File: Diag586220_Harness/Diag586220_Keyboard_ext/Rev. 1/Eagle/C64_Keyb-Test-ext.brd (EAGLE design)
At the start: 22 x 55 mm, 16 parts, among them IC1 4066N, IC2 4066N, J1 BL1-85AXX-20U, Q1 BC547B

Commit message: Silk Screen Update
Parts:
- added U$19: OPEN_SOURCE_HW, Logo:OPENHW
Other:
- board text added: "http://github.com/svenpetersen1965"
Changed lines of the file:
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@@
 <layer number="21" name="tPlace" color="7" fill="1" visible="yes" active="yes"/>
 <layer number="22" name="bPlace" color="7" fill="1" visible="no" active="yes"/>
-<layer number="23" name="tOrigins" color="15" fill="1" visible="yes" active="yes"/>
+<layer number="23" name="tOrigins" color="15" fill="1" visible="no" active="yes"/>
 <layer number="24" name="bOrigins" color="15" fill="1" visible="no" active="yes"/>
 <layer number="25" name="tNames" color="7" fill="1" visible="yes" active="yes"/>
@@
 <layer number="45" name="Holes" color="7" fill="1" visible="yes" active="yes"/>
 <layer number="46" name="Milling" color="3" fill="1" visible="no" active="yes"/>
-<layer number="47" name="Measures" color="7" fill="1" visible="no" active="yes"/>
+<layer number="47" name="Measures" color="7" fill="1" visible="yes" active="yes"/>
 <layer number="48" name="Document" color="5" fill="1" visible="yes" active="yes"/>
 <layer number="49" name="Reference" color="7" fill="1" visible="yes" active="yes"/>
@@
 <layer number="250" name="Descript" color="7" fill="1" visible="no" active="no"/>
 <layer number="251" name="SMDround" color="7" fill="1" visible="no" active="no"/>
+<layer number="252" name="BR-BS" color="7" fill="1" visible="no" active="yes"/>
+<layer number="253" name="BR-LS" color="7" fill="1" visible="no" active="yes"/>
 <layer number="254" name="OrgLBR" color="7" fill="1" visible="no" active="no"/>
 <layer number="255" name="Accent" color="7" fill="1" visible="yes" active="yes"/>
@@
 <text x="15.24" y="2.69875" size="1.016" layer="25">4k7</text>
 <text x="15.24" y="0.3175" size="1.016" layer="25">1k</text>
+<text x="2.54" y="39.52875" size="1.016" layer="22" rot="MR270">http://github.com/svenpetersen1965</text>
 </plain>
 <attributes>
@@
 <attribute name="VALUE" x="6.82625" y="51.1175" size="1.27" layer="27"/>
 </element>
+<element name="U$19" library="Logo" package="OPENHW" value="OPEN_SOURCE_HW" x="17.30375" y="3.96875" smashed="yes" rot="MR0"/>
 </elements>
 <signals>

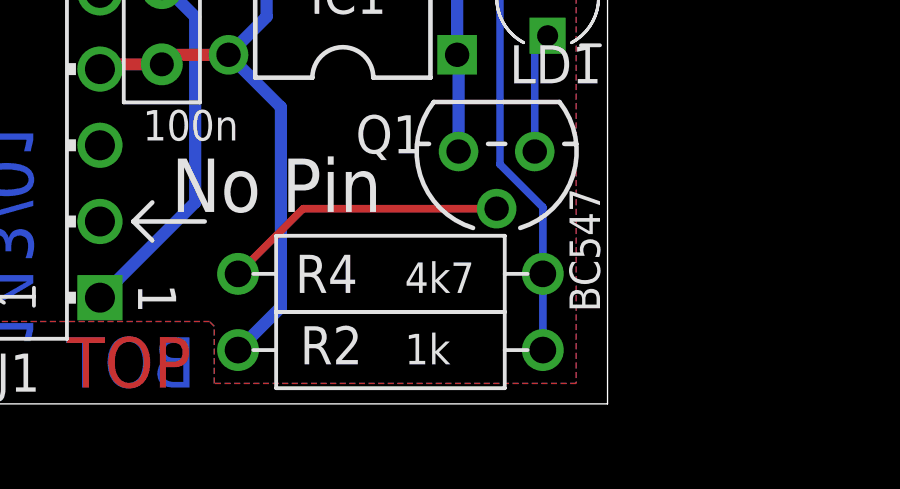
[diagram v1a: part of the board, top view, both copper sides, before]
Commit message: BOM v1.1
R2 and R4 values are changed
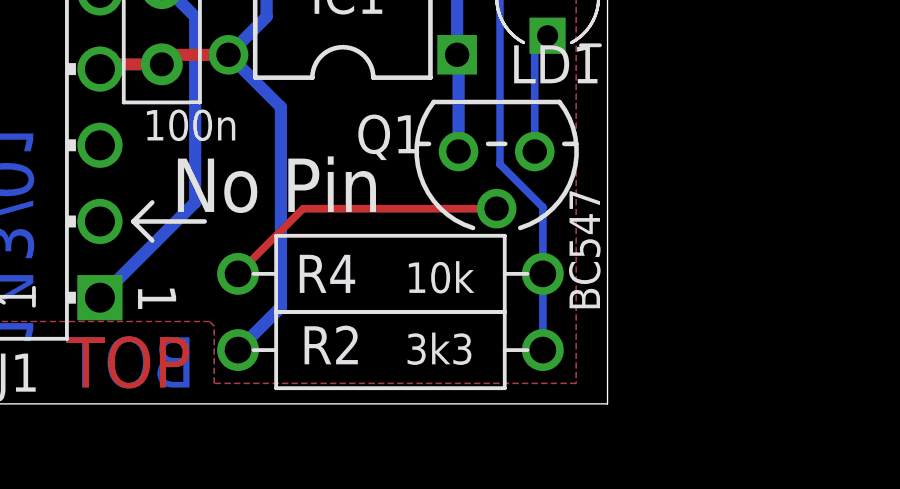
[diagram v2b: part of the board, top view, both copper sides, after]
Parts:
- R2: value 1k -> 3k3
- R4: value 4k7 -> 10k
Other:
- board text added: "3k3"
- board text removed: "1k"
- board text removed: "4k7"
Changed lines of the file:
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@@
 <?xml version="1.0" encoding="utf-8"?>
 <!DOCTYPE eagle SYSTEM "eagle.dtd">
-<eagle version="9.5.2">
+<eagle version="9.6.2">
 <drawing>
 <settings>
@@
 <layer number="21" name="tPlace" color="7" fill="1" visible="yes" active="yes"/>
 <layer number="22" name="bPlace" color="7" fill="1" visible="no" active="yes"/>
-<layer number="23" name="tOrigins" color="15" fill="1" visible="no" active="yes"/>
+<layer number="23" name="tOrigins" color="15" fill="1" visible="yes" active="yes"/>
 <layer number="24" name="bOrigins" color="15" fill="1" visible="no" active="yes"/>
 <layer number="25" name="tNames" color="7" fill="1" visible="yes" active="yes"/>
@@
 <layer number="28" name="bValues" color="7" fill="1" visible="no" active="yes"/>
 <layer number="29" name="tStop" color="7" fill="3" visible="no" active="yes"/>
-<layer number="30" name="bStop" color="7" fill="6" visible="no" active="yes"/>
+<layer number="30" name="bStop" color="7" fill="6" visible="yes" active="yes"/>
 <layer number="31" name="tCream" color="7" fill="4" visible="no" active="yes"/>
 <layer number="32" name="bCream" color="7" fill="5" visible="no" active="yes"/>
@@
 <text x="13.97" y="27.14625" size="1.016" layer="25" rot="R90">100n</text>
 <text x="21.74875" y="2.06375" size="1.016" layer="25" rot="R90">BC547</text>
-<text x="15.24" y="2.69875" size="1.016" layer="25">4k7</text>
-<text x="15.24" y="0.3175" size="1.016" layer="25">1k</text>
+<text x="15.24" y="2.69875" size="1.016" layer="25">10k</text>
+<text x="15.24" y="0.3175" size="1.016" layer="25">3k3</text>
 <text x="2.54" y="39.52875" size="1.016" layer="22" rot="MR270">http://github.com/svenpetersen1965</text>
 </plain>
@@
 <attribute name="VALUE" x="14.605" y="50.32375" size="1.27" layer="27" rot="R180"/>
 </element>
-<element name="R2" library="DISCRETE" package="R-10" value="1k" x="14.76375" y="0.79375" smashed="yes" rot="R180">
+<element name="R2" library="DISCRETE" package="R-10" value="3k3" x="14.76375" y="0.79375" smashed="yes" rot="R180">
 <attribute name="NAME" x="11.7475" y="0.3175" size="1.27" layer="25"/>
 <attribute name="VALUE" x="17.93875" y="1.42875" size="1.27" layer="27" rot="R180"/>
@@
 </element>
 <element name="U$17" library="Logo" package="SVEN_TAG" value="" x="2.06375" y="23.97125" smashed="yes"/>
-<element name="R4" library="DISCRETE" package="R-10" value="4k7" x="14.76375" y="3.33375" smashed="yes">
+<element name="R4" library="DISCRETE" package="R-10" value="10k" x="14.76375" y="3.33375" smashed="yes">
 <attribute name="NAME" x="11.58875" y="2.69875" size="1.27" layer="25"/>
 <attribute name="VALUE" x="11.58875" y="2.69875" size="1.27" layer="27"/>
